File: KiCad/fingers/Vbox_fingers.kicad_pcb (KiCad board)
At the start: 2 copper layers, 109 x 45 mm, 20 parts, among them J1 Conn_01x10, J2 Conn_01x10, SW1 SW_Push_45deg, SW10 SW_Push_45deg, SW11 SW_Push_45deg, SW12 SW_Push_45deg, SW13 SW_Push_45deg, SW14 SW_Push_45deg, SW15 SW_Push_45deg, SW16 SW_Push_45deg, SW17 SW_Push_45deg, SW18 SW_Push_45deg, SW2 SW_Push_45deg, SW3 SW_Push_45deg, SW4 SW_Push_45deg, SW5 SW_Push_45deg, SW6 SW_Push_45deg, SW7 SW_Push_45deg, SW8 SW_Push_45deg, SW9 SW_Push_45deg

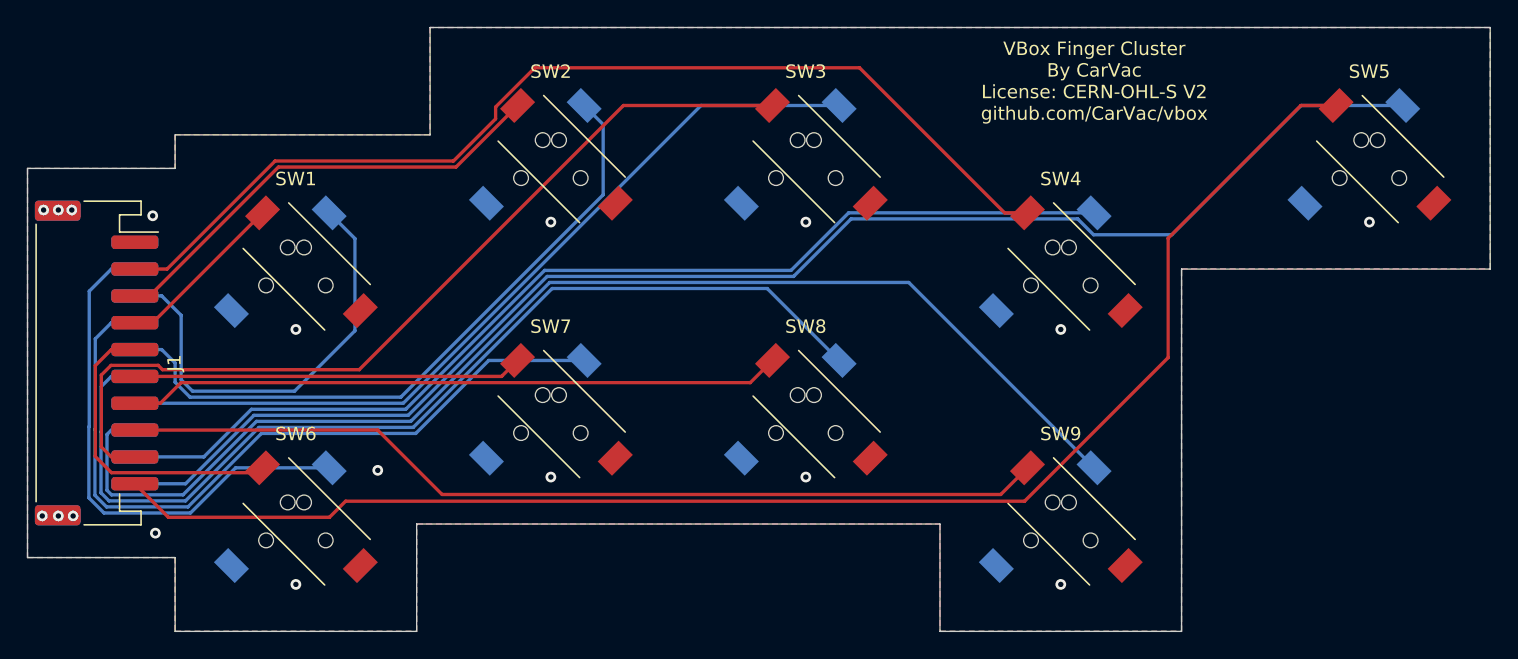
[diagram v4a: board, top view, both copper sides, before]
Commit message: move traces away from hand solder pads
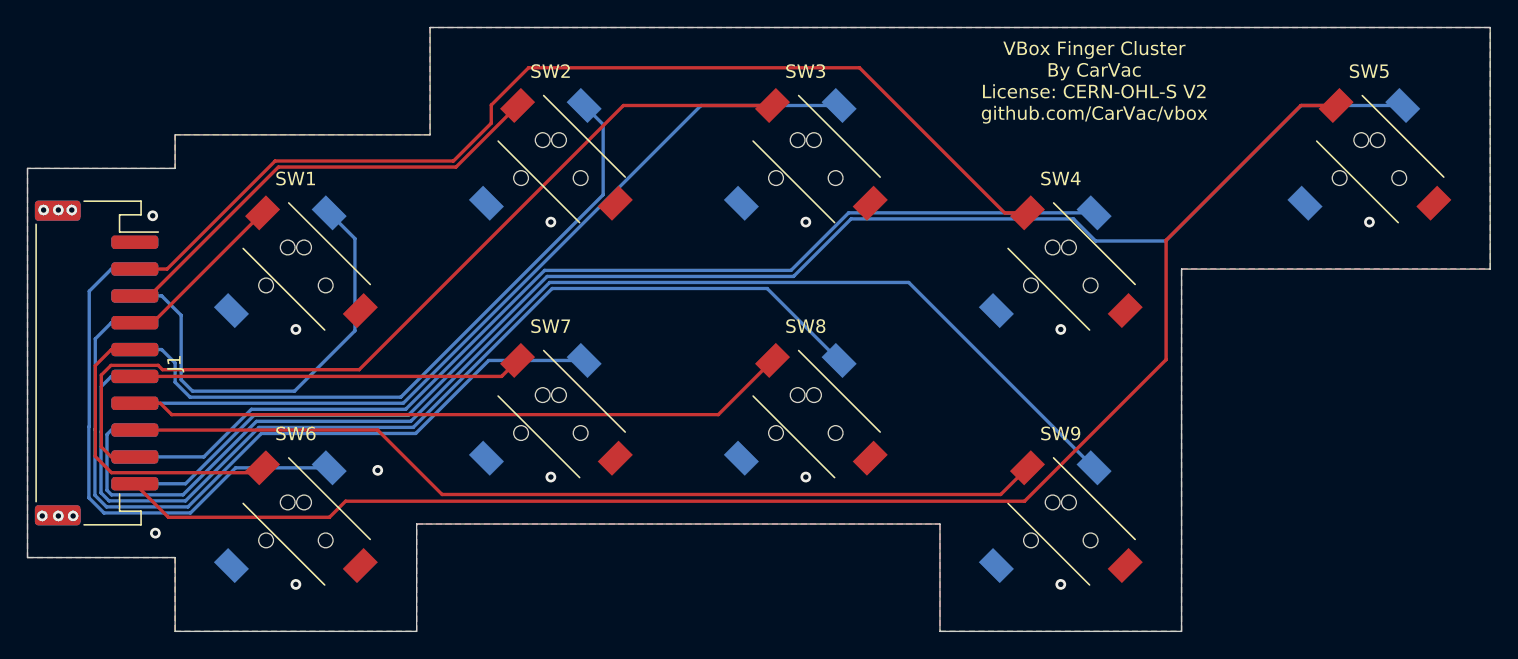
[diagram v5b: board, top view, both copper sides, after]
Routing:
- net DOWN: track 48.8 -> 49.5 mm
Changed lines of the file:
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@@
   (via (at 82.3 119.4) (size 0.8) (drill 0.4) (layers "F.Cu" "B.Cu") (net 1))
   (via (at 157 105.5) (size 0.8) (drill 0.4) (layers "F.Cu" "B.Cu") (free) (net 1))
-  (segment (start 174.889051 88.810949) (end 165 98.7) (width 0.25) (layer "F.Cu") (net 2))
-  (segment (start 165 98.7) (end 165 107.6) (width 0.25) (layer "F.Cu") (net 2))
   (segment (start 102.5 119.5) (end 90.5 119.5) (width 0.25) (layer "F.Cu") (net 2))
+  (segment (start 90.5 119.5) (end 88 117) (width 0.25) (layer "F.Cu") (net 2))
   (segment (start 103.7 118.3) (end 102.5 119.5) (width 0.25) (layer "F.Cu") (net 2))
+  (segment (start 164.85 107.75) (end 154.3 118.3) (width 0.25) (layer "F.Cu") (net 2))
   (segment (start 177.518056 88.810949) (end 174.889051 88.810949) (width 0.25) (layer "F.Cu") (net 2))
-  (segment (start 90.5 119.5) (end 88 117) (width 0.25) (layer "F.Cu") (net 2))
   (segment (start 154.3 118.3) (end 103.7 118.3) (width 0.25) (layer "F.Cu") (net 2))
-  (segment (start 165 107.6) (end 154.3 118.3) (width 0.25) (layer "F.Cu") (net 2))
+  (segment (start 164.85 98.85) (end 164.85 107.75) (width 0.25) (layer "F.Cu") (net 2))
+  (segment (start 174.889051 88.810949) (end 164.85 98.85) (width 0.25) (layer "F.Cu") (net 2))
   (segment (start 88 113) (end 106.1 113) (width 0.25) (layer "F.Cu") (net 3))
   (segment (start 106.1 113) (end 110.9 117.8) (width 0.25) (layer "F.Cu") (net 3))
   (segment (start 110.9 117.8) (end 152.529005 117.8) (width 0.25) (layer "F.Cu") (net 3))
   (segment (start 152.529005 117.8) (end 154.518056 115.810949) (width 0.25) (layer "F.Cu") (net 3))
-  (segment (start 89.9 111) (end 91.433112 109.466888) (width 0.25) (layer "F.Cu") (net 4))
-  (segment (start 91.433112 109.466888) (end 133.862117 109.466888) (width 0.25) (layer "F.Cu") (net 4))
+  (segment (start 90.75 111.85) (end 131.479005 111.85) (width 0.25) (layer "F.Cu") (net 4))
   (segment (start 88 111) (end 89.9 111) (width 0.25) (layer "F.Cu") (net 4))
-  (segment (start 133.862117 109.466888) (end 135.518056 107.810949) (width 0.25) (layer "F.Cu") (net 4))
+  (segment (start 131.479005 111.85) (end 135.518056 107.810949) (width 0.25) (layer "F.Cu") (net 4))
+  (segment (start 89.9 111) (end 90.75 111.85) (width 0.25) (layer "F.Cu") (net 4))
   (segment (start 88 109) (end 115.329005 109) (width 0.25) (layer "F.Cu") (net 5))
   (segment (start 115.329005 109) (end 116.518056 107.810949) (width 0.25) (layer "F.Cu") (net 5))
@@
   (segment (start 89.1 103) (end 98.7 93.4) (width 0.25) (layer "F.Cu") (net 9))
   (segment (start 88 103) (end 89.1 103) (width 0.25) (layer "F.Cu") (net 9))
-  (segment (start 114.884908 88.923815) (end 117.808723 86) (width 0.25) (layer "F.Cu") (net 10))
+  (segment (start 90.4 101) (end 98.45 92.95) (width 0.25) (layer "F.Cu") (net 10))
+  (segment (start 114.56 90.132609) (end 114.56 88.78) (width 0.25) (layer "F.Cu") (net 10))
   (segment (start 152.810949 96.810949) (end 154.518056 96.810949) (width 0.25) (layer "F.Cu") (net 10))
+  (segment (start 88 101) (end 90.4 101) (width 0.25) (layer "F.Cu") (net 10))
+  (segment (start 117.34 86) (end 142 86) (width 0.25) (layer "F.Cu") (net 10))
+  (segment (start 114.56 88.78) (end 117.34 86) (width 0.25) (layer "F.Cu") (net 10))
+  (segment (start 142 86) (end 152.810949 96.810949) (width 0.25) (layer "F.Cu") (net 10))
+  (segment (start 111.742609 92.95) (end 114.56 90.132609) (width 0.25) (layer "F.Cu") (net 10))
   (segment (start 98.45 92.95) (end 111.742609 92.95) (width 0.25) (layer "F.Cu") (net 10))
-  (segment (start 117.808723 86) (end 142 86) (width 0.25) (layer "F.Cu") (net 10))
-  (segment (start 90.4 101) (end 98.45 92.95) (width 0.25) (layer "F.Cu") (net 10))
-  (segment (start 111.742609 92.95) (end 114.884908 89.807701) (width 0.25) (layer "F.Cu") (net 10))
-  (segment (start 88 101) (end 90.4 101) (width 0.25) (layer "F.Cu") (net 10))
-  (segment (start 142 86) (end 152.810949 96.810949) (width 0.25) (layer "F.Cu") (net 10))
-  (segment (start 114.884908 89.807701) (end 114.884908 88.923815) (width 0.25) (layer "F.Cu") (net 10))
   (segment (start 95.50985 115.810949) (end 102.481944 115.810949) (width 0.25) (layer "B.Cu") (net 11))
   (segment (start 84.6 112.740812) (end 84.575 112.765812) (width 0.25) (layer "B.Cu") (net 11))
@@
   (segment (start 108 111) (end 130.189051 88.810949) (width 0.25) (layer "B.Cu") (net 16))
   (segment (start 88 111) (end 108 111) (width 0.25) (layer "B.Cu") (net 16))
+  (segment (start 159.6 98.91) (end 164.81 98.91) (width 0.25) (layer "B.Cu") (net 17))
+  (segment (start 164.81 98.91) (end 174.909051 88.810949) (width 0.25) (layer "B.Cu") (net 17))
+  (segment (start 108.372792 111.9) (end 118.722792 101.55) (width 0.25) (layer "B.Cu") (net 17))
   (segment (start 88 117) (end 91.775215 117) (width 0.25) (layer "B.Cu") (net 17))
-  (segment (start 158.260949 97.260949) (end 159.444097 98.444097) (width 0.25) (layer "B.Cu") (net 17))
-  (segment (start 165.275903 98.444097) (end 174.909051 88.810949) (width 0.25) (layer "B.Cu") (net 17))
   (segment (start 174.909051 88.810949) (end 182.481944 88.810949) (width 0.25) (layer "B.Cu") (net 17))
+  (segment (start 157.950949 97.260949) (end 159.6 98.91) (width 0.25) (layer "B.Cu") (net 17))
   (segment (start 91.775215 117) (end 96.875215 111.9) (width 0.25) (layer "B.Cu") (net 17))
+  (segment (start 141.375447 97.260949) (end 157.950949 97.260949) (width 0.25) (layer "B.Cu") (net 17))
+  (segment (start 118.722792 101.55) (end 137.086396 101.55) (width 0.25) (layer "B.Cu") (net 17))
   (segment (start 137.086396 101.55) (end 141.375447 97.260949) (width 0.25) (layer "B.Cu") (net 17))
-  (segment (start 159.444097 98.444097) (end 165.275903 98.444097) (width 0.25) (layer "B.Cu") (net 17))
-  (segment (start 108.372792 111.9) (end 118.722792 101.55) (width 0.25) (layer "B.Cu") (net 17))
   (segment (start 96.875215 111.9) (end 108.372792 111.9) (width 0.25) (layer "B.Cu") (net 17))
-  (segment (start 141.375447 97.260949) (end 158.260949 97.260949) (width 0.25) (layer "B.Cu") (net 17))
-  (segment (start 118.722792 101.55) (end 137.086396 101.55) (width 0.25) (layer "B.Cu") (net 17))
   (segment (start 86.261826 117.825) (end 91.586611 117.825) (width 0.25) (layer "B.Cu") (net 18))
   (segment (start 86.25 113) (end 85.925 113.325) (width 0.25) (layer "B.Cu") (net 18))

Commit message: make both sides share holes
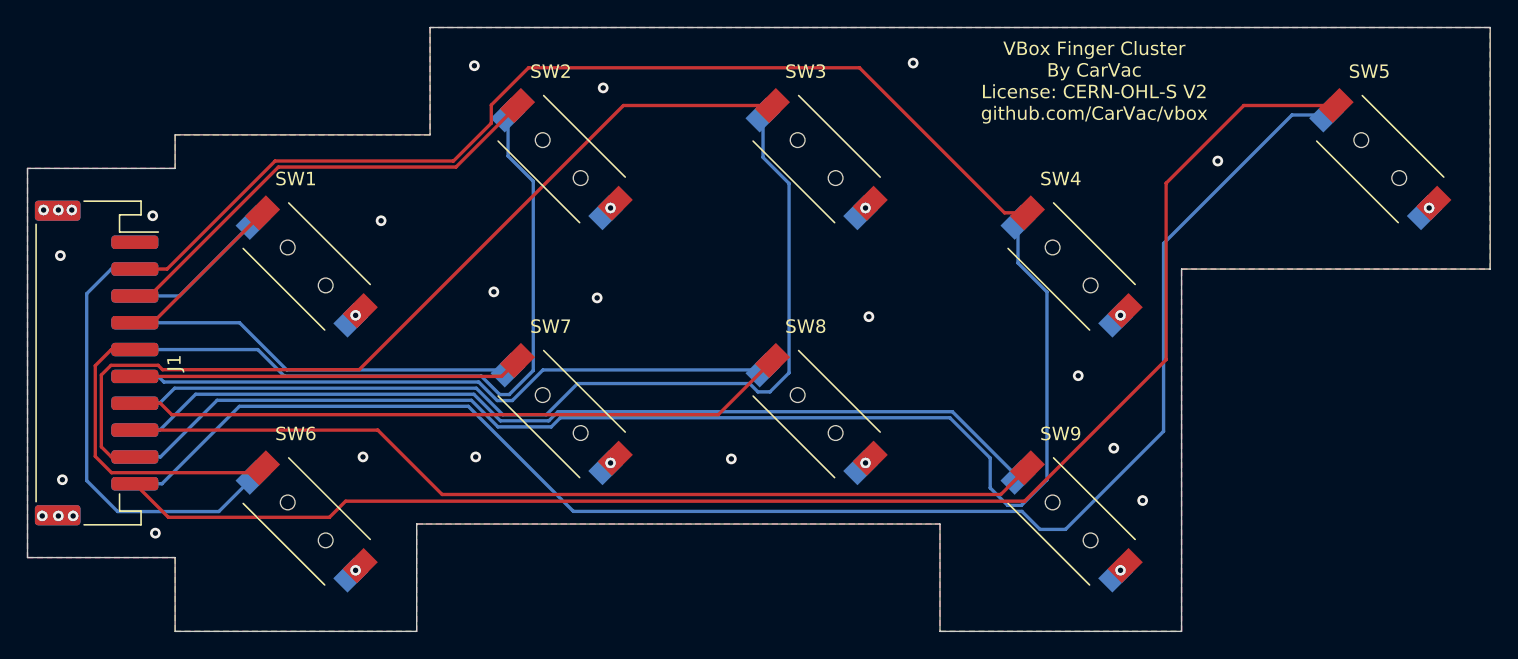
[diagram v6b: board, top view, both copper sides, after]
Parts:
- SW10, SW11, SW12, SW13, SW14, SW15, SW16, SW17, SW18: footprint Buttons:Vbox -> Buttons:Vbox_1
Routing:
- net Z: track 56.5 -> 29.3 mm
- net X: track 74.8 -> 48.5 mm
- net MS: track 33.6 -> 11.1 mm
- net B: track 92.3 -> 70.0 mm
- net R: track 79.0 -> 95.7 mm
- net Y: track 61.7 -> 71.9 mm
- net RIGHTSTART: track 107.5 -> 116.0 mm
- net UP: track 39.3 -> 32.7 mm
- net START: track 108.5 -> 111.0 mm
- net LS: track 50.7 -> 51.6 mm
- net GND: vias 18 -> 33

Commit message: flip connectors
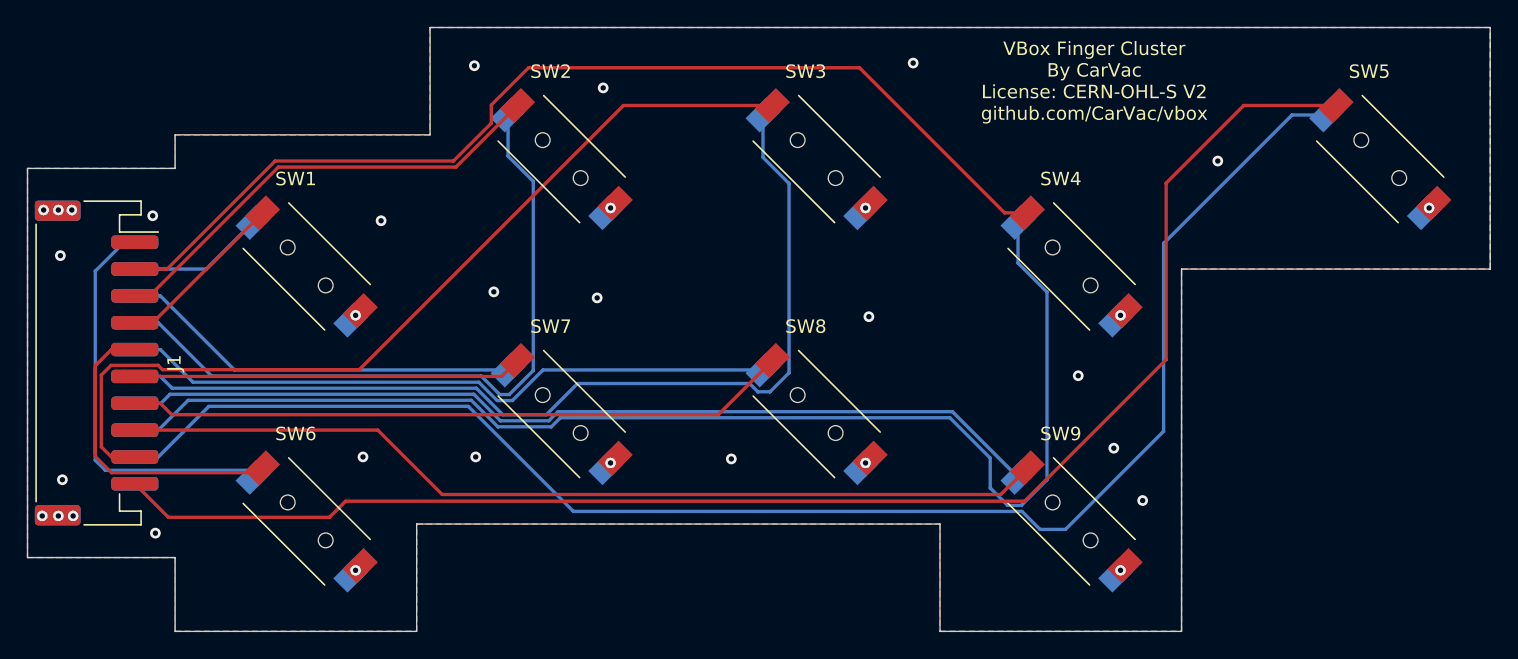
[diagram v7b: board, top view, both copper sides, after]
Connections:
- J1 pad MP: GND -> (no net)
- J2 pad 1: RIGHTSTART -> GND
- J2 pad 10: GND -> UP
- J2 pad 2: R -> RIGHTSTART
- J2 pad 3: B -> R
- J2 pad 4: Y -> B
- J2 pad 5: X -> Y
- J2 pad 6: LS -> X
- J2 pad 7: Z -> LS
- J2 pad 8: MS -> Z
- J2 pad 9: UP -> MS
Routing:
- net UP: track 32.7 -> 30.2 mm
- net X: track 48.5 -> 49.3 mm
- net RIGHTSTART: track 116.0 -> 115.2 mm
- net B: track 70.0 -> 69.2 mm
- net MS: track 11.1 -> 10.3 mm
- net Z: track 29.3 -> 30.1 mm
- net R: track 95.7 -> 94.9 mm
- net LS: track 51.6 -> 52.5 mm
